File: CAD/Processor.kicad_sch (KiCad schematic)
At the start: 77 parts, among them M1 FID, M11 MOUNTING, M15 MOUNTING, M2 FID, M3 MOUNTING, M9 MOUNTING, U11 ATSAME70Q20B-ANT, X1 ECS-120-10-33B-CKM-TR

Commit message: Update to KiCad 10.0
Update to 10.0. Several kicad library footprints changed, so some traces had to be rerouted.
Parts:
- TM1, TM2: value ~ -> (none)

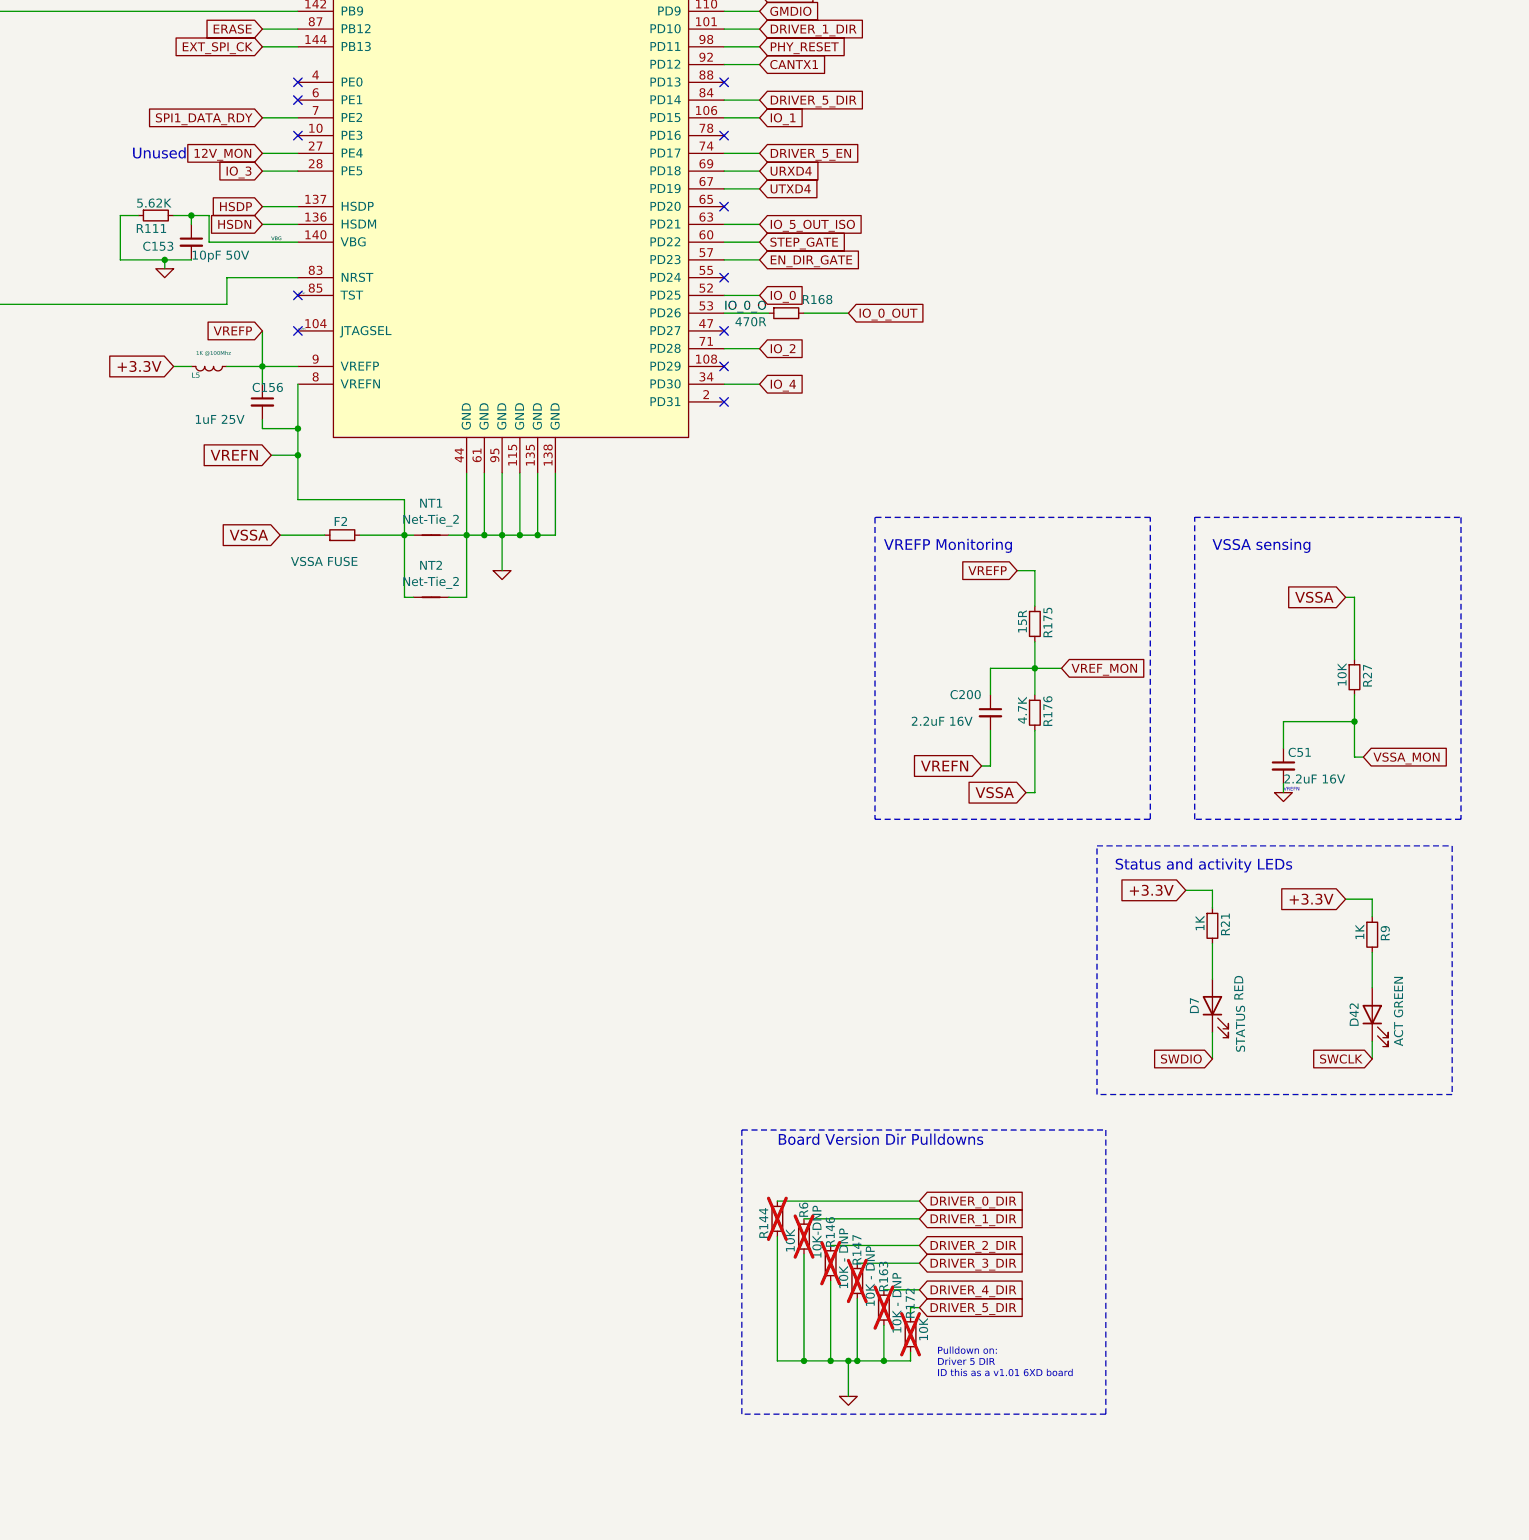
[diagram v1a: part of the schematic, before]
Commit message: Add versioning resistors + V12 enable from MCU + Misc.
Re added the resistors that told the firmware which hardware revision the board is.
Changed V12 circuit to add a V12 Monitor line and allow the V12 converter to be enabled from the MCU.
Moved clamping and pull up circuits for IO_0 -> IO_4 to allow more room next to 2x25 Pin Socket.
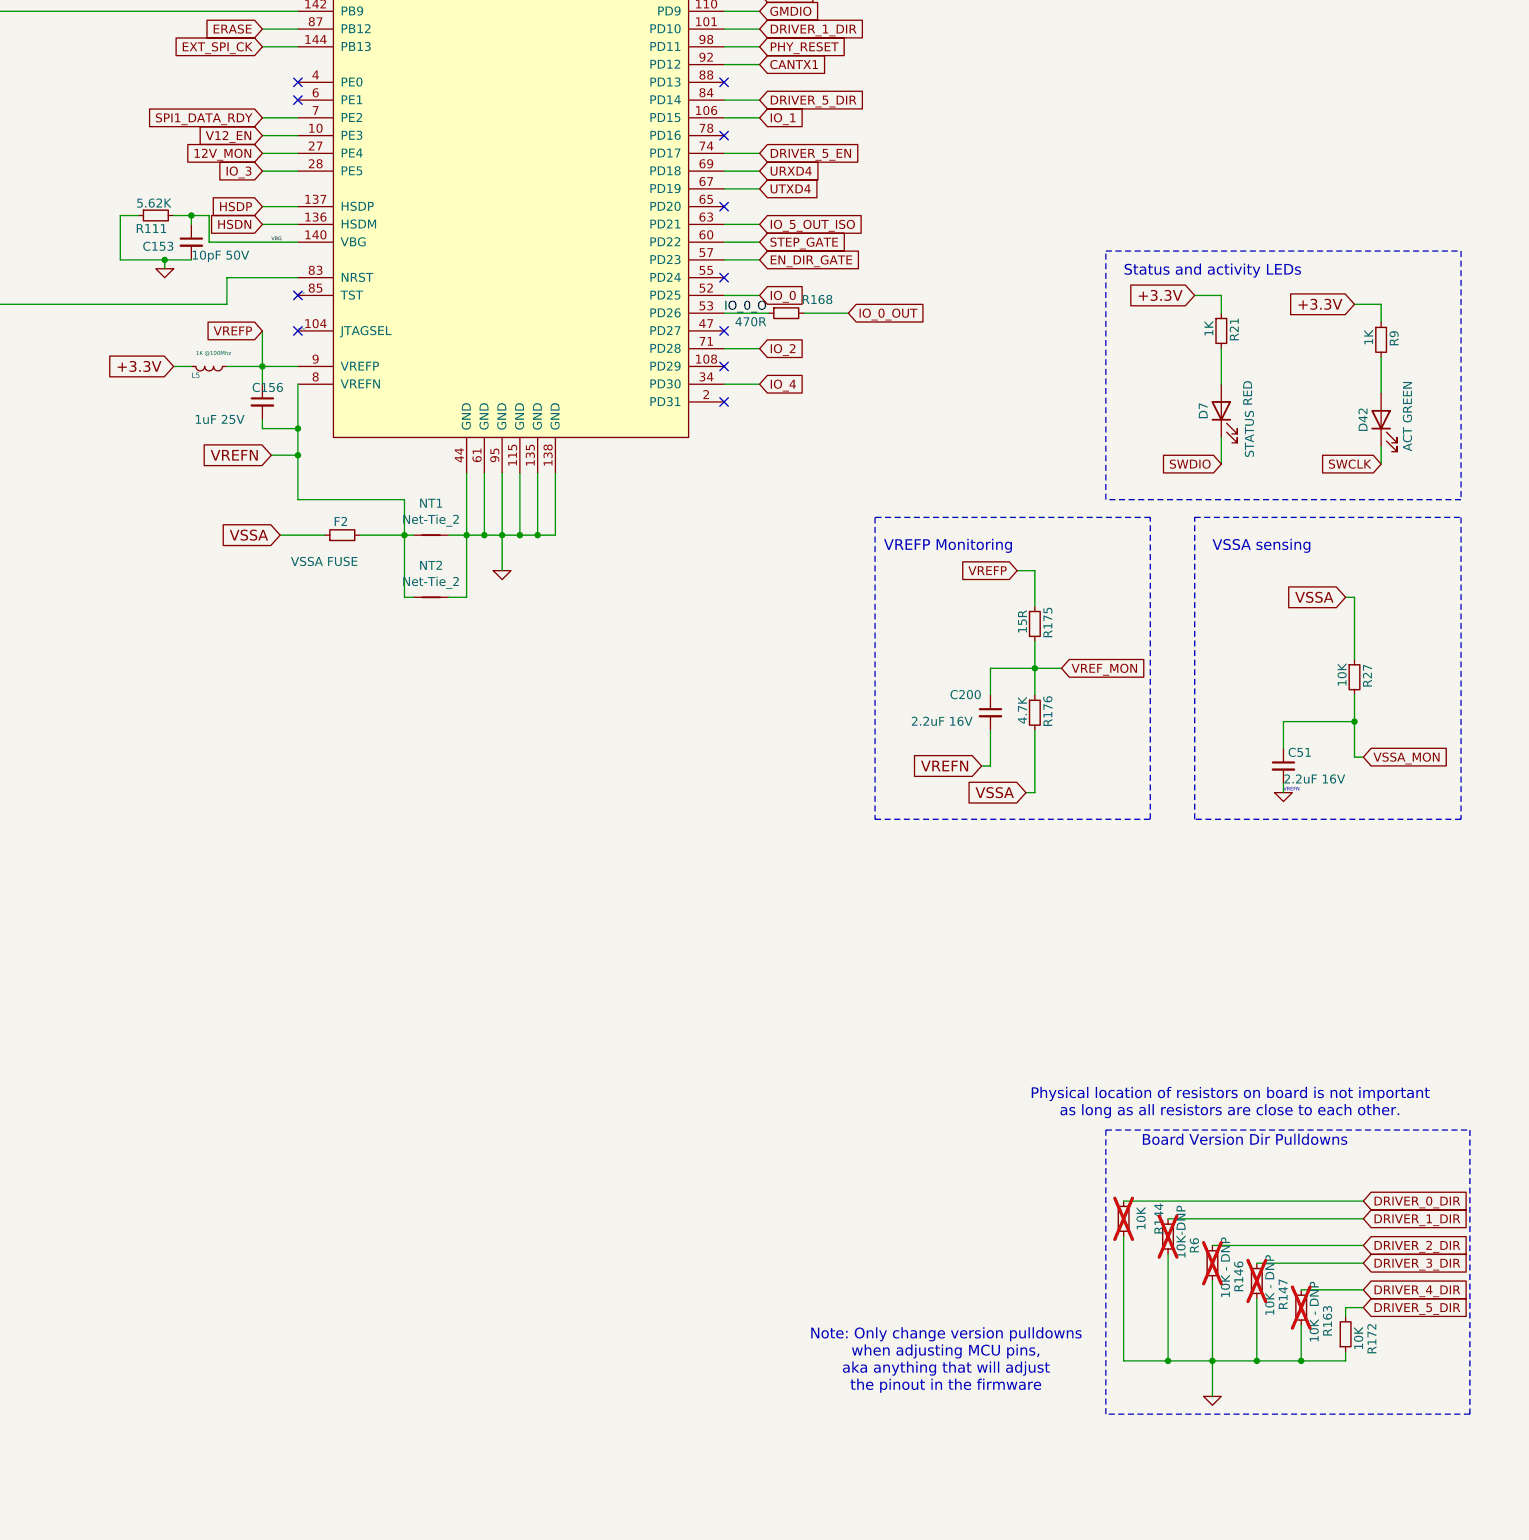
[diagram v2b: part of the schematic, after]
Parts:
- R172: footprint Resistor_SMD:R_0402_1005Metric_Wbry -> 3DPotter:0402_1005Metric_NoSilk; now fitted; now in the parts list
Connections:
- net V12_EN: now reaches U11.10 (PE3)
- no-connect marks 35 -> 34
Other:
- note added: "Note: Only change version pulldowns when adjusting MCU pins, aka anything that will adjust the pinout in the firmware"
- note added: "Physical location of resistors on board is not important as long as all resistors are close to each other."
- note removed: "Pulldown on: Driver 5 DIR ID this as a v1.01 6XD board"
- note removed: "Unused"
- moved on the sheet: D42, D7, R144, R146, R147, R163, R21, R6, R9
